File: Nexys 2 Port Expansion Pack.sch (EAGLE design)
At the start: 24 parts, among them IC1 74HC245N, IC2 74HC245N, IC3 74HC245N

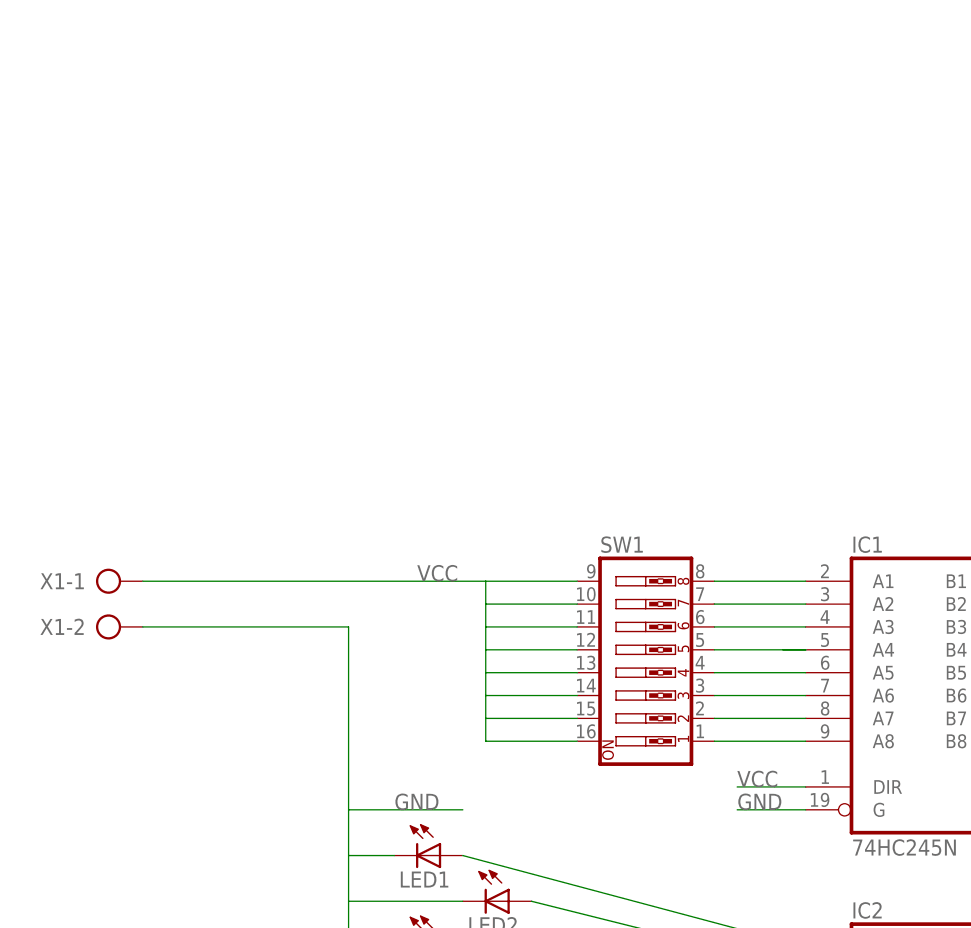
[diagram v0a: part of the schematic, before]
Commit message: Add resistence to the dipswitch
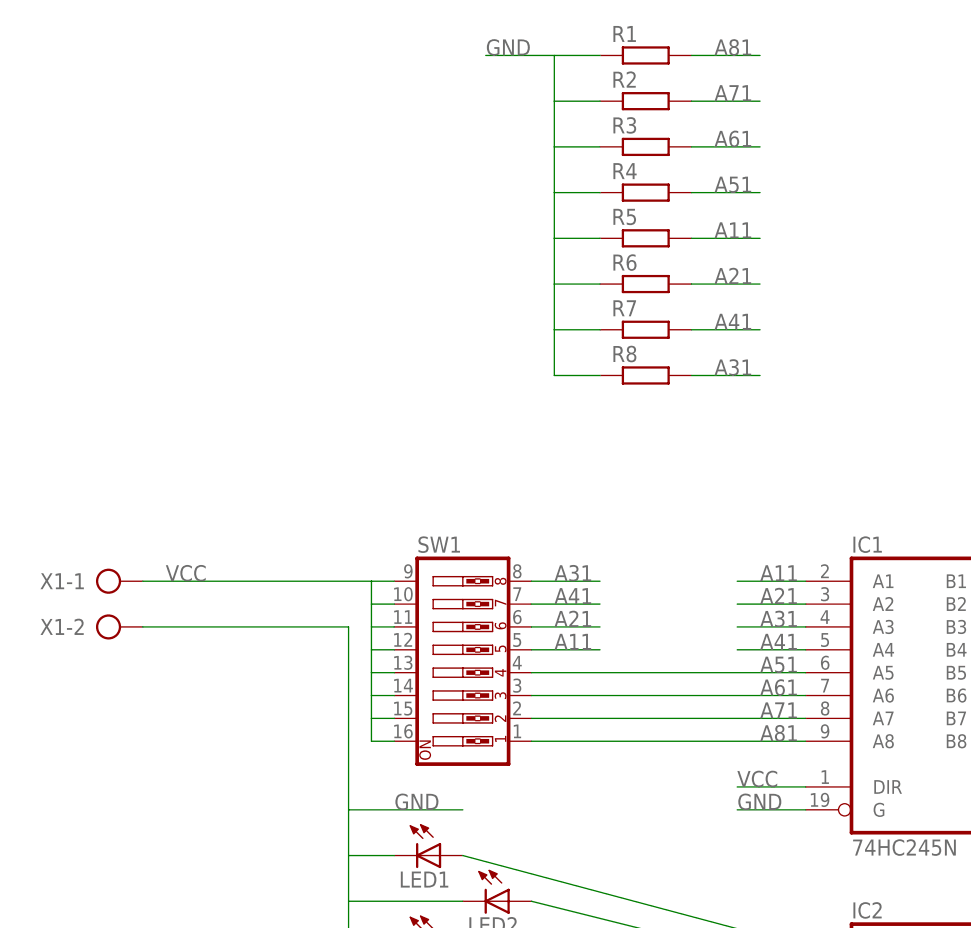
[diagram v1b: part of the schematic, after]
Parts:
- added R1, R2, R3, R4, R5, R6, R7, R8: (no value), resistor:R-EU_0207/15
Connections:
- removed net N$1: IC1A.A1, SW1.8
- removed net N$2: IC1A.A2, SW1.7
- removed net N$3: IC1A.A3, SW1.6
- removed net N$4: IC1A.A4, SW1.5
- removed net N$5: IC1A.A5, SW1.4
- removed net N$6: IC1A.A6, SW1.3
- removed net N$7: IC1A.A7, SW1.2
- removed net N$8: IC1A.A8, SW1.1
- new net A11: IC1A.A1, R5.2, SW1.5
- new net A21: IC1A.A2, R6.2, SW1.6
- new net A31: IC1A.A3, R8.2, SW1.8
- new net A41: IC1A.A4, R7.2, SW1.7
- new net A51: IC1A.A5, R4.2, SW1.4
- new net A61: IC1A.A6, R3.2, SW1.3
- new net A71: IC1A.A7, R2.2, SW1.2
- new net A81: IC1A.A8, R1.2, SW1.1
- net GND: now also R1.1, R2.1, R3.1, R4.1, R5.1, R6.1, R7.1, R8.1
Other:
- moved on the sheet: SW1
